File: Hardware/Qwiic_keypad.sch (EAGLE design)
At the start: 26 parts, among them J3 PTH, J6 AVR_SPI_PROG_3X2TESTPOINTS, U3 ATTINY84

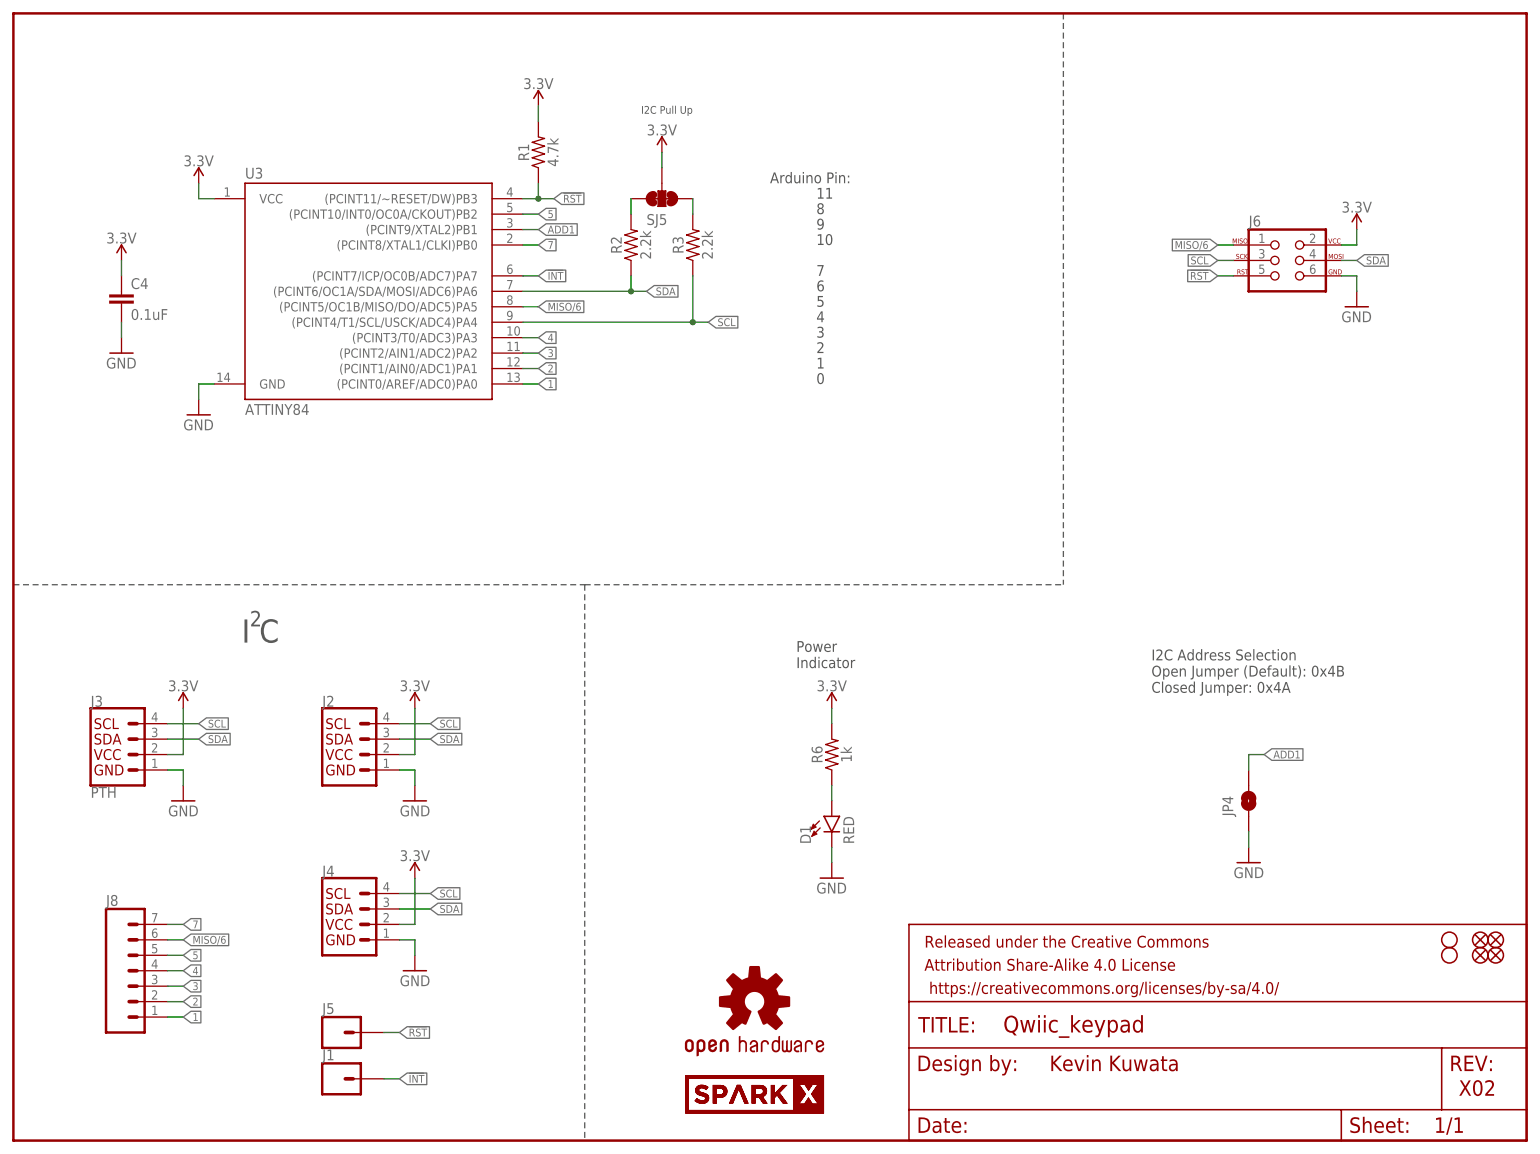
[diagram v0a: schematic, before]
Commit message: updating hardware
-SFE logo in schematic (w/ slight re-arrange to fit)

-changed version in sch (and brd) to v10

-bumped traces up from 6 mils to 8 mils.

-bumped vias up from 12 mils to 15 mils.

-switched to "sfe tight" drc

-minor trace nudgeing to avoid clearance warnings.

-increased "pass through" 3.3V trace to 16 mils. added more GND vias.
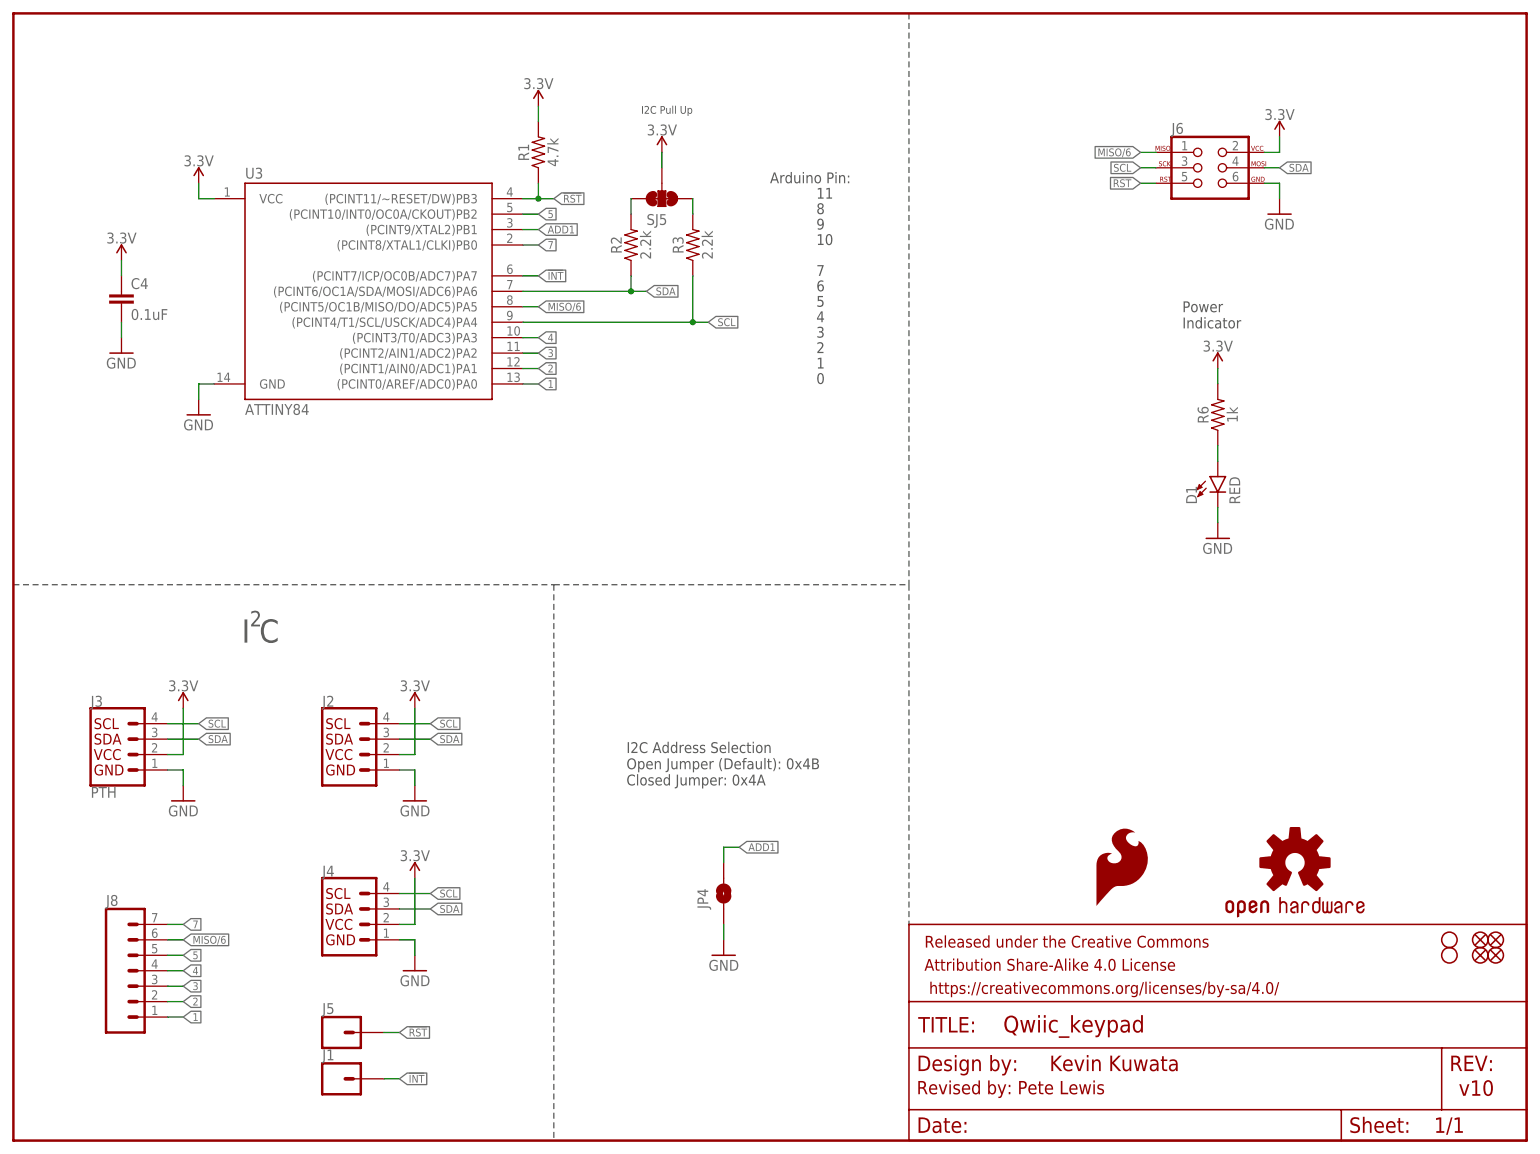
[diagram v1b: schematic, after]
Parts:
- removed U$1, U$2: SPARKX-LOGO3, SparkX:SPARKX-LOGO3
- added LOGO3: SFE_LOGO_FLAME.1_INCH, SparkFun-Aesthetics:SFE_LOGO_FLAME.1_INCH
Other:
- note added: "Revised by: Pete Lewis"
- note added: "v10"
- note removed: "X02"
- moved on the sheet: D1, J6, JP4, R6

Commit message: Locking footprint on 1x7 connector to keypad
This will help with holding position during selective solder
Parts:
- J8: device SparkFun-Connectors:CONN_07NO_SILK -> SparkFun-Connectors:CONN_07LOCK_NO_SILK
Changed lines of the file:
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@@
 <?xml version="1.0" encoding="utf-8"?>
 <!DOCTYPE eagle SYSTEM "eagle.dtd">
-<eagle version="6.5.0">
+<eagle version="9.2.2">
 <drawing>
 <settings>
-<setting alwaysvectorfont="yes"/>
+<setting alwaysvectorfont="no"/>
+<setting keepoldvectorfont="yes"/>
 <setting verticaltext="up"/>
 </settings>
@@
 <part name="H1" library="SparkFun-Hardware" deviceset="STAND-OFF" device=""/>
 <part name="H2" library="SparkFun-Hardware" deviceset="STAND-OFF" device=""/>
-<part name="J8" library="SparkFun-Connectors" deviceset="CONN_07" device="NO_SILK"/>
+<part name="J8" library="SparkFun-Connectors" deviceset="CONN_07" device="LOCK_NO_SILK"/>
 <part name="R2" library="SparkFun-Resistors" deviceset="2.2KOHM" device="-0603-1/10W-1%" value="2.2k"/>
 <part name="R3" library="SparkFun-Resistors" deviceset="2.2KOHM" device="-0603-1/10W-1%" value="2.2k"/>
@@
 <instance part="H1" gate="G$1" x="236.22" y="33.02" smashed="yes"/>
 <instance part="H2" gate="G$1" x="236.22" y="30.48" smashed="yes"/>
-<instance part="J8" gate="G$1" x="20.32" y="25.4" smashed="yes">
+<instance part="J8" gate="J1" x="20.32" y="25.4" smashed="yes">
 <attribute name="VALUE" x="15.24" y="15.494" size="1.778" layer="96" font="vector"/>
 <attribute name="NAME" x="15.24" y="38.608" size="1.778" layer="95" font="vector"/>
@@
 <attribute name="VALUE" x="106.68" y="165.354" size="1.778" layer="96" align="bottom-center"/>
 </instance>
-<instance part="LOGO3" gate="G$1" x="177.8" y="38.1"/>
+<instance part="LOGO3" gate="G$1" x="177.8" y="38.1" smashed="yes"/>
 </instances>
 <busses>
@@
 <wire x1="25.4" y1="27.94" x2="27.94" y2="27.94" width="0.1524" layer="91"/>
 <label x="27.94" y="27.94" size="1.27" layer="95" xref="yes"/>
-<pinref part="J8" gate="G$1" pin="4"/>
+<pinref part="J8" gate="J1" pin="4"/>
 </segment>
 <segment>
@@
 <wire x1="25.4" y1="25.4" x2="27.94" y2="25.4" width="0.1524" layer="91"/>
 <label x="27.94" y="25.4" size="1.27" layer="95" xref="yes"/>
-<pinref part="J8" gate="G$1" pin="3"/>
+<pinref part="J8" gate="J1" pin="3"/>
 </segment>
 <segment>
@@
 <wire x1="25.4" y1="22.86" x2="27.94" y2="22.86" width="0.1524" layer="91"/>
 <label x="27.94" y="22.86" size="1.27" layer="95" xref="yes"/>
-<pinref part="J8" gate="G$1" pin="2"/>
+<pinref part="J8" gate="J1" pin="2"/>
 </segment>
 <segment>
@@
 <wire x1="25.4" y1="20.32" x2="27.94" y2="20.32" width="0.1524" layer="91"/>
 <label x="27.94" y="20.32" size="1.27" layer="95" xref="yes"/>
-<pinref part="J8" gate="G$1" pin="1"/>
+<pinref part="J8" gate="J1" pin="1"/>
 </segment>
 <segment>
@@
 <wire x1="25.4" y1="33.02" x2="27.94" y2="33.02" width="0.1524" layer="91"/>
 <label x="27.94" y="33.02" size="1.27" layer="95" xref="yes"/>
-<pinref part="J8" gate="G$1" pin="6"/>
+<pinref part="J8" gate="J1" pin="6"/>
 </segment>
 <segment>
@@
 <wire x1="25.4" y1="35.56" x2="27.94" y2="35.56" width="0.1524" layer="91"/>
 <label x="27.94" y="35.56" size="1.27" layer="95" xref="yes"/>
-<pinref part="J8" gate="G$1" pin="7"/>
+<pinref part="J8" gate="J1" pin="7"/>
 </segment>
 </net>
@@
 <wire x1="25.4" y1="30.48" x2="27.94" y2="30.48" width="0.1524" layer="91"/>
 <label x="27.94" y="30.48" size="1.27" layer="95" xref="yes"/>
-<pinref part="J8" gate="G$1" pin="5"/>
-</segment>
-</net>
+<pinref part="J8" gate="J1" pin="5"/>
+</segment>
+</net>

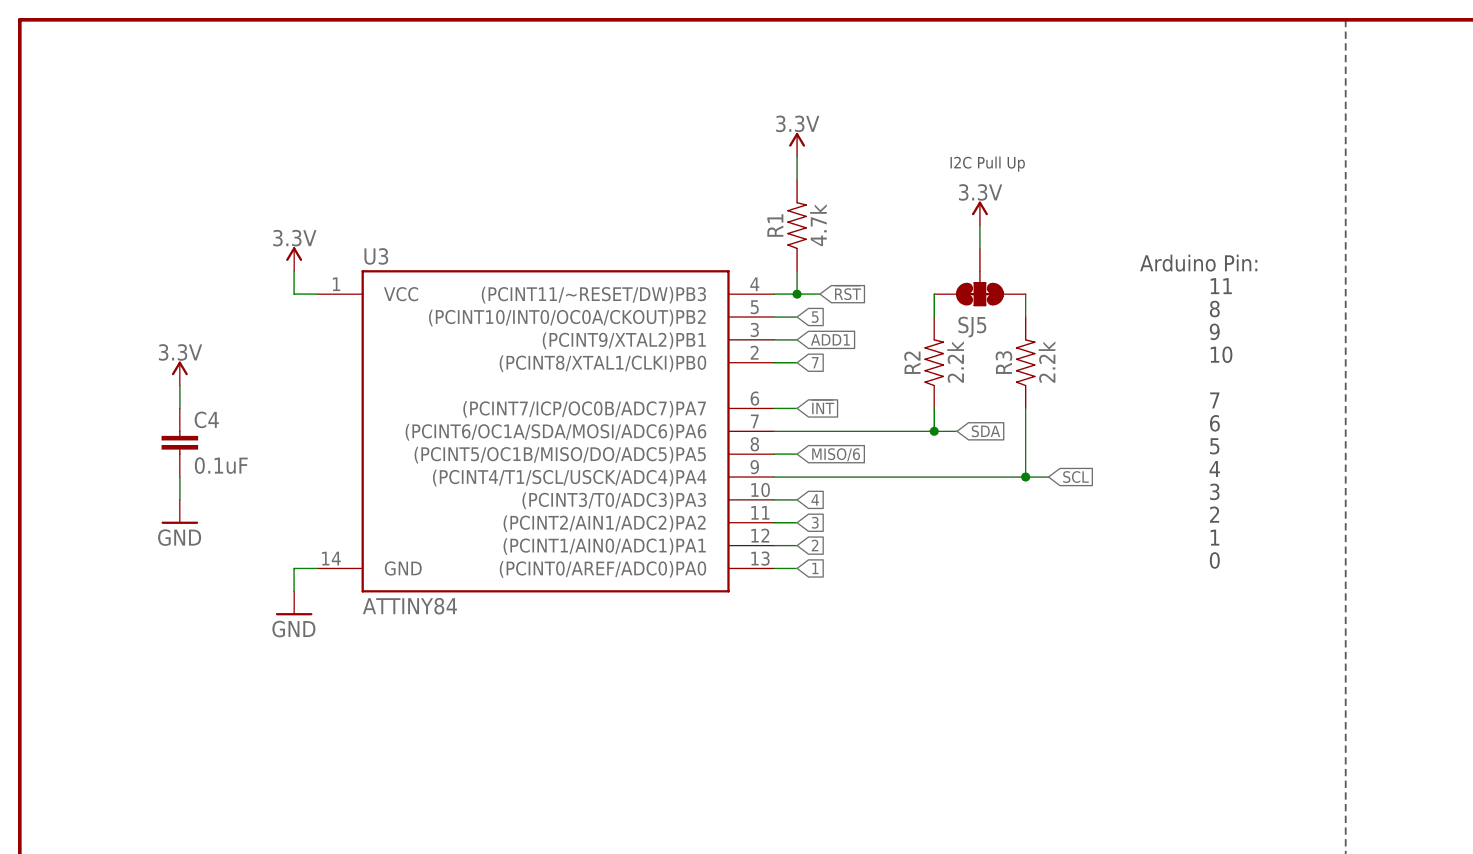
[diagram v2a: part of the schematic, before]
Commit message: added INT pullup resistor
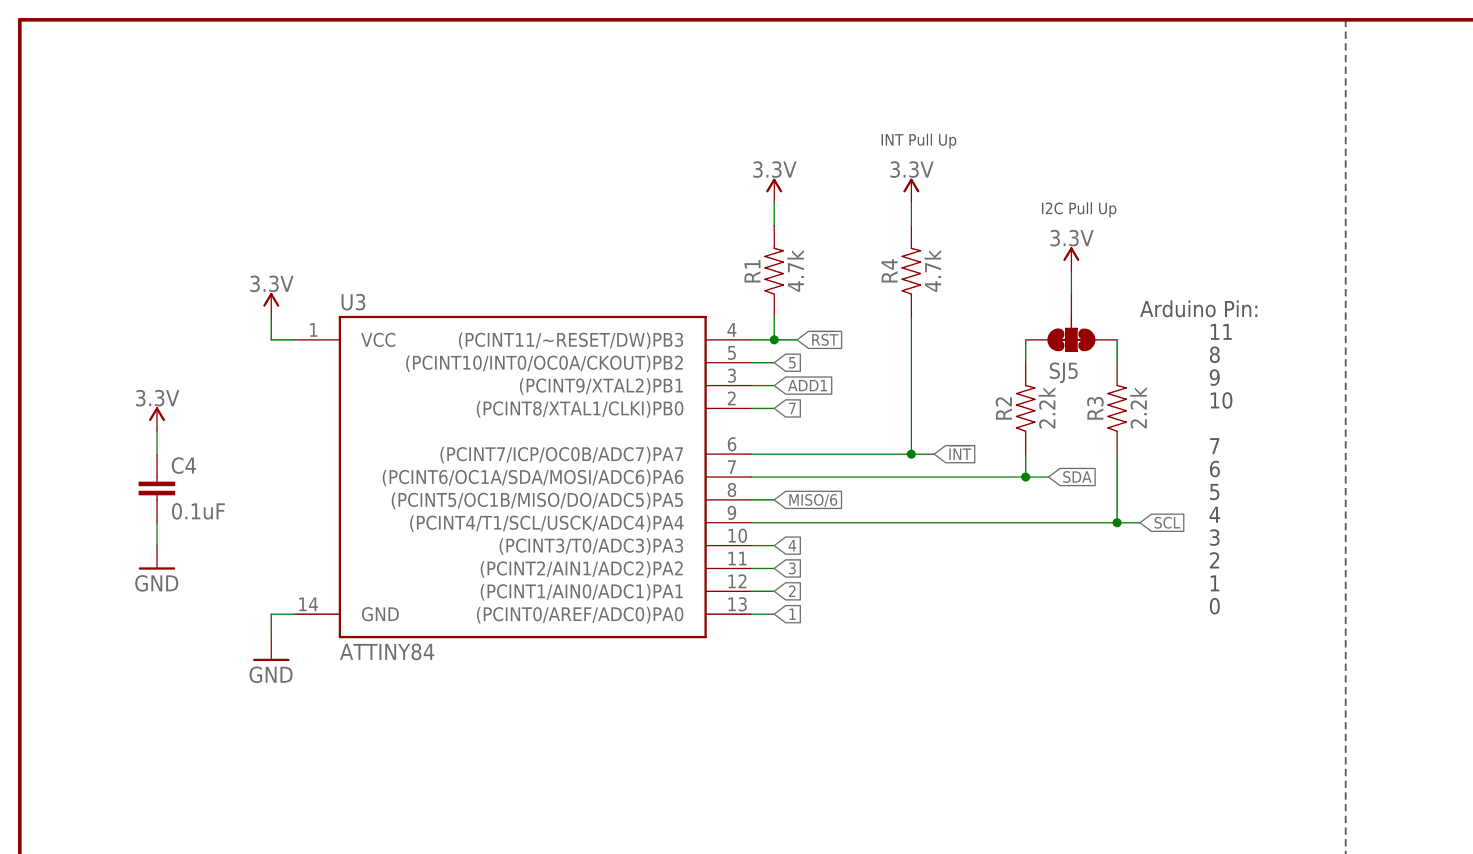
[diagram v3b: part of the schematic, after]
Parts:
- added R4: 4.7k, SparkFun-Resistors:4.7KOHM-0603-1/10W-1%
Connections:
- net !INT: now also R4.1
- net 3.3V: now also R4.2
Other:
- note added: "INT Pull Up"
- moved on the sheet: C4, R1, R2, R3, SJ5, U3
